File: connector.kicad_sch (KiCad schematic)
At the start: 4 parts, among them J1 Conn_01x04_Pin

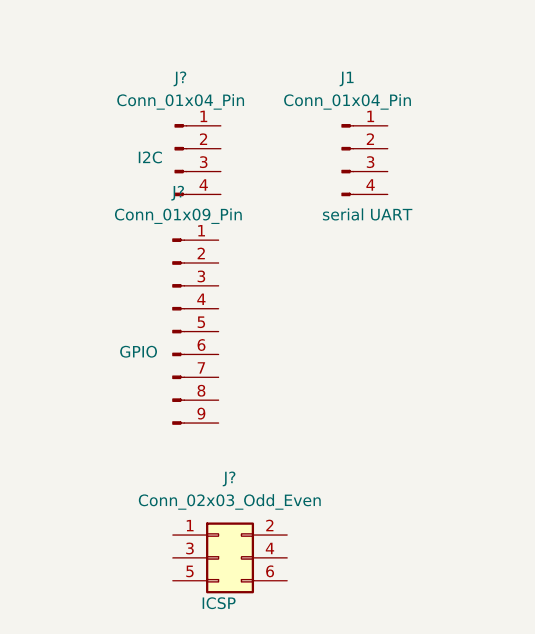
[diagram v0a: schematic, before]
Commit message: symbols arranged
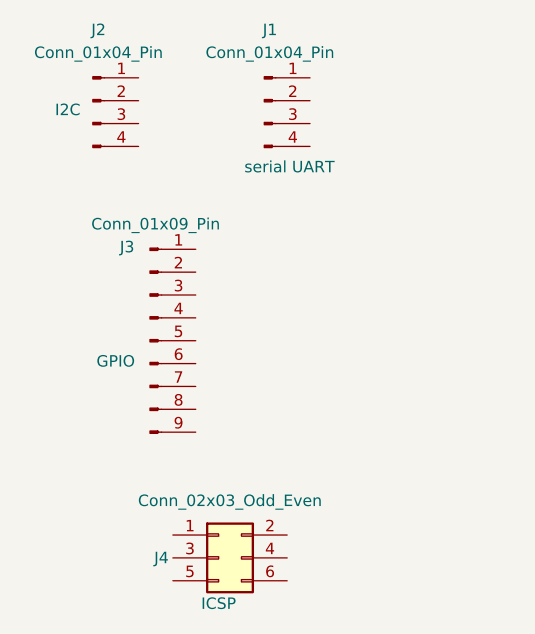
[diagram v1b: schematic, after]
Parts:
- gave numbers to parts that had none: 3
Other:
- moved on the sheet: J1, J2, J3
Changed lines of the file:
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@@
 	(symbol
 		(lib_id "Connector:Conn_01x04_Pin")
-		(at 89.154 66.294 0)
-		(unit 1)
-		(exclude_from_sim no)
-		(in_bom yes)
-		(on_board yes)
-		(dnp no)
-		(property "Reference" "J?"
-			(at 89.789 58.42 0)
+		(at 80.01 60.96 0)
+		(unit 1)
+		(exclude_from_sim no)
+		(in_bom yes)
+		(on_board yes)
+		(dnp no)
+		(property "Reference" "J2"
+			(at 80.645 53.086 0)
 			(effects
 				(font
@@
 		)
 		(property "Value" "Conn_01x04_Pin"
-			(at 89.789 60.96 0)
-			(effects
-				(font
-					(size 1.27 1.27)
-				)
-			)
-		)
-		(property "Footprint" ""
-			(at 89.154 66.294 0)
-			(effects
-				(font
-					(size 1.27 1.27)
-				)
-				(hide yes)
-			)
-		)
-		(property "Datasheet" "~"
-			(at 89.154 66.294 0)
+			(at 80.645 55.626 0)
+			(effects
+				(font
+					(size 1.27 1.27)
+				)
+			)
+		)
+		(property "Footprint" ""
+			(at 80.01 60.96 0)
+			(effects
+				(font
+					(size 1.27 1.27)
+				)
+				(hide yes)
+			)
+		)
+		(property "Datasheet" "~"
+			(at 80.01 60.96 0)
 			(effects
 				(font
@@
 		)
 		(property "Description" "Generic connector, single row, 01x04, script generated"
-			(at 89.154 66.294 0)
+			(at 80.01 60.96 0)
 			(effects
 				(font
@@
 		)
 		(property "purpose" "I2C"
-			(at 86.36 67.31 0)
+			(at 77.216 61.976 0)
 			(effects
 				(font
@@
 			(project ""
 				(path "/3b0fcfdb-a6be-445d-b7c4-9e7a0848a48e/4dcddee0-74b0-4b70-a68e-7c337efdec33"
-					(reference "J?")
+					(reference "J2")
 					(unit 1)
 				)
@@
 	(symbol
 		(lib_id "Connector:Conn_01x09_Pin")
-		(at 88.9 86.614 0)
-		(unit 1)
-		(exclude_from_sim no)
-		(in_bom yes)
-		(on_board yes)
-		(dnp no)
-		(property "Reference" "J?"
-			(at 89.535 71.12 0)
+		(at 86.36 87.63 0)
+		(unit 1)
+		(exclude_from_sim no)
+		(in_bom yes)
+		(on_board yes)
+		(dnp no)
+		(property "Reference" "J3"
+			(at 83.82 77.216 0)
 			(effects
 				(font
@@
 		)
 		(property "Value" "Conn_01x09_Pin"
-			(at 89.535 73.66 0)
-			(effects
-				(font
-					(size 1.27 1.27)
-				)
-			)
-		)
-		(property "Footprint" ""
-			(at 88.9 86.614 0)
-			(effects
-				(font
-					(size 1.27 1.27)
-				)
-				(hide yes)
-			)
-		)
-		(property "Datasheet" "~"
-			(at 88.9 86.614 0)
+			(at 86.995 74.676 0)
+			(effects
+				(font
+					(size 1.27 1.27)
+				)
+			)
+		)
+		(property "Footprint" ""
+			(at 86.36 87.63 0)
+			(effects
+				(font
+					(size 1.27 1.27)
+				)
+				(hide yes)
+			)
+		)
+		(property "Datasheet" "~"
+			(at 86.36 87.63 0)
 			(effects
 				(font
@@
 		)
 		(property "Description" "Generic connector, single row, 01x09, script generated"
-			(at 88.9 86.614 0)
+			(at 86.36 87.63 0)
 			(effects
 				(font
@@
 		)
 		(property "PURPOSE" "GPIO"
-			(at 85.09 88.9 0)
+			(at 82.55 89.916 0)
 			(effects
 				(font
@@
 			(project ""
 				(path "/3b0fcfdb-a6be-445d-b7c4-9e7a0848a48e/4dcddee0-74b0-4b70-a68e-7c337efdec33"
-					(reference "J?")
+					(reference "J3")
 					(unit 1)
 				)
@@
 		(on_board yes)
 		(dnp no)
-		(property "Reference" "J?"
-			(at 95.25 102.87 0)
+		(property "Reference" "J4"
+			(at 87.63 111.76 0)
 			(effects
 				(font
@@
 			(project ""
 				(path "/3b0fcfdb-a6be-445d-b7c4-9e7a0848a48e/4dcddee0-74b0-4b70-a68e-7c337efdec33"
-					(reference "J?")
+					(reference "J4")
 					(unit 1)
 				)
@@
 	(symbol
 		(lib_id "Connector:Conn_01x04_Pin")
-		(at 107.696 66.294 0)
+		(at 99.06 60.96 0)
 		(unit 1)
 		(exclude_from_sim no)
@@
 		(dnp no)
 		(property "Reference" "J1"
-			(at 108.331 58.42 0)
+			(at 99.695 53.086 0)
 			(effects
 				(font
@@
 		)
 		(property "Value" "Conn_01x04_Pin"
-			(at 108.331 60.96 0)
-			(effects
-				(font
-					(size 1.27 1.27)
-				)
-			)
-		)
-		(property "Footprint" ""
-			(at 107.696 66.294 0)
-			(effects
-				(font
-					(size 1.27 1.27)
-				)
-				(hide yes)
-			)
-		)
-		(property "Datasheet" "~"
-			(at 107.696 66.294 0)
+			(at 99.695 55.626 0)
+			(effects
+				(font
+					(size 1.27 1.27)
+				)
+			)
+		)
+		(property "Footprint" ""
+			(at 99.06 60.96 0)
+			(effects
+				(font
+					(size 1.27 1.27)
+				)
+				(hide yes)
+			)
+		)
+		(property "Datasheet" "~"
+			(at 99.06 60.96 0)
 			(effects
 				(font
@@
 		)
 		(property "Description" "Generic connector, single row, 01x04, script generated"
-			(at 107.696 66.294 0)
+			(at 99.06 60.96 0)
 			(effects
 				(font
@@
 		)
 		(property "purpose" "serial UART"
-			(at 110.49 73.66 0)
-			(effects
-				(font
+			(at 101.854 68.326 0)
+			(effects
+				(font

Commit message: Footprints Associated
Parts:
- J1, J2: footprint (none) -> Connector_PinHeader_2.54mm:PinHeader_1x04_P2.54mm_Vertical
- J3: footprint (none) -> Connector_PinHeader_2.54mm:PinHeader_1x09_P2.54mm_Vertical
- J4: footprint (none) -> Connector_PinHeader_2.54mm:PinHeader_2x03_P2.54mm_Vertical
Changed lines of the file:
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@@
 			)
 		)
-		(property "Footprint" ""
+		(property "Footprint" "Connector_PinHeader_2.54mm:PinHeader_1x04_P2.54mm_Vertical"
 			(at 80.01 60.96 0)
 			(effects
@@
 			)
 		)
-		(property "Footprint" ""
+		(property "Footprint" "Connector_PinHeader_2.54mm:PinHeader_1x09_P2.54mm_Vertical"
 			(at 86.36 87.63 0)
 			(effects
@@
 			)
 		)
-		(property "Footprint" ""
+		(property "Footprint" "Connector_PinHeader_2.54mm:PinHeader_2x03_P2.54mm_Vertical"
 			(at 93.98 111.76 0)
 			(effects
@@
 			)
 		)
-		(property "Footprint" ""
+		(property "Footprint" "Connector_PinHeader_2.54mm:PinHeader_1x04_P2.54mm_Vertical"
 			(at 99.06 60.96 0)
 			(effects

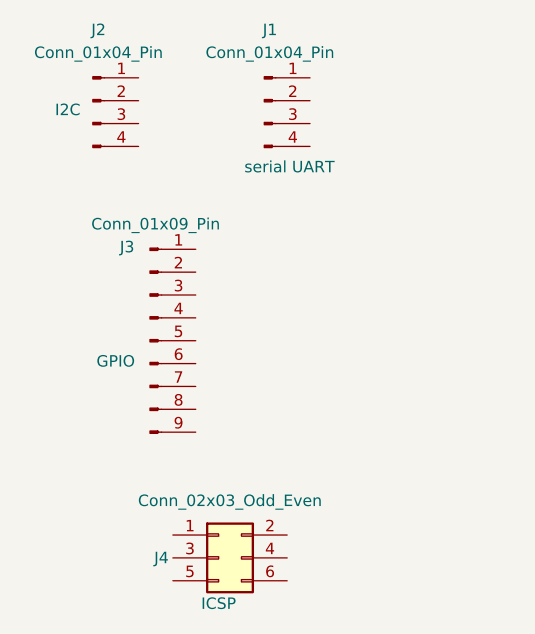
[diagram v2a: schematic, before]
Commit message: COMPLETED THE WIRING AND RESOLVED ERC ERRORS SUCH AS POWER PIN ASSIGNMENT AND THE MCU UNIT SYMBOL TYPE(INPUT,OUTPUT,PASSIVE ETC
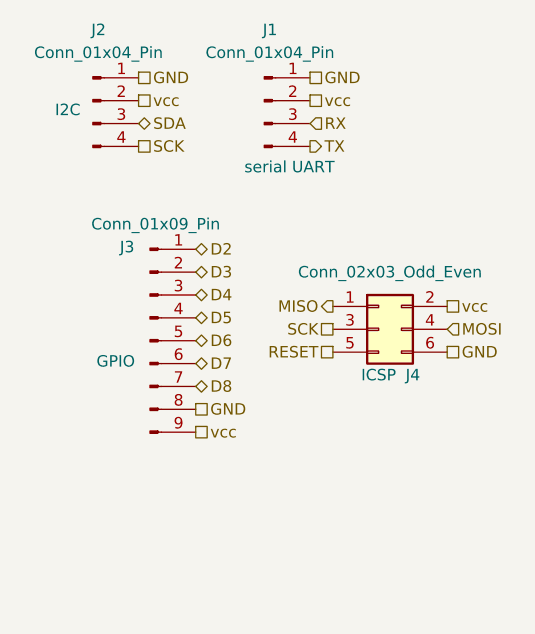
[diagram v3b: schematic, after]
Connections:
- net GND: now reaches J2.1 (Pin_1)
- net GND: now also J1.1 (Pin_1), J3.8 (Pin_8), J4.6 (Pin_6)
- net vcc: now reaches J2.2 (Pin_2)
- net vcc: now also J1.2 (Pin_2), J3.9 (Pin_9), J4.2 (Pin_2)
- net SDA: now reaches J2.3 (Pin_3)
- net SCK: now reaches J2.4 (Pin_4)
- net SCK: now also J4.3 (Pin_3)
- net D2: now reaches J3.1 (Pin_1)
- net D3: now reaches J3.2 (Pin_2)
- net D4: now reaches J3.3 (Pin_3)
- net D5: now reaches J3.4 (Pin_4)
- net D6: now reaches J3.5 (Pin_5)
- net D7: now reaches J3.6 (Pin_6)
- net D8: now reaches J3.7 (Pin_7)
- net MISO: now reaches J4.1 (Pin_1)
- net MOSI: now reaches J4.4 (Pin_4)
- net RESET: now reaches J4.5 (Pin_5)
- net RX: now reaches J1.3 (Pin_3)
- net TX: now reaches J1.4 (Pin_4)
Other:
- moved on the sheet: J4

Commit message: fixed two defects in schematic
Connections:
- net SCK: no longer J2.4 (Pin_4)
- new net SCL: J2.4 (Pin_4)
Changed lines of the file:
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@@
+		)
+	)
+	(hierarchical_label "SCL"
+		(shape passive)
+		(at 85.09 66.04 0)
+		(effects
+			(font
+				(size 1.27 1.27)
+			)
+			(justify left)
 		)
 	)
@@
 		(effects
 			(font
-				(size 1.27 1.27)
-			)
-			(justify left)
-		)
-	)
-	(hierarchical_label "SCK"
-		(shape passive)
-		(at 85.09 66.04 0)
-		(effects
-			(font
